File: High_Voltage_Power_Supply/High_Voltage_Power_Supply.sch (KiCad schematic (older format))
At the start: 108 parts, among them J1 Conn_01x02_Female, J2 Conn_01x02_Female, J3 Conn_01x02_Female, J4 Conn_01x12_Female, Q1 Q_NMOS_GDS, Q2 Q_NMOS_GDS, Q3 Q_NMOS_GDS, Q4 Q_NIGBT_GCE, U1 LT3751-TSSOP, U10 ADR3412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

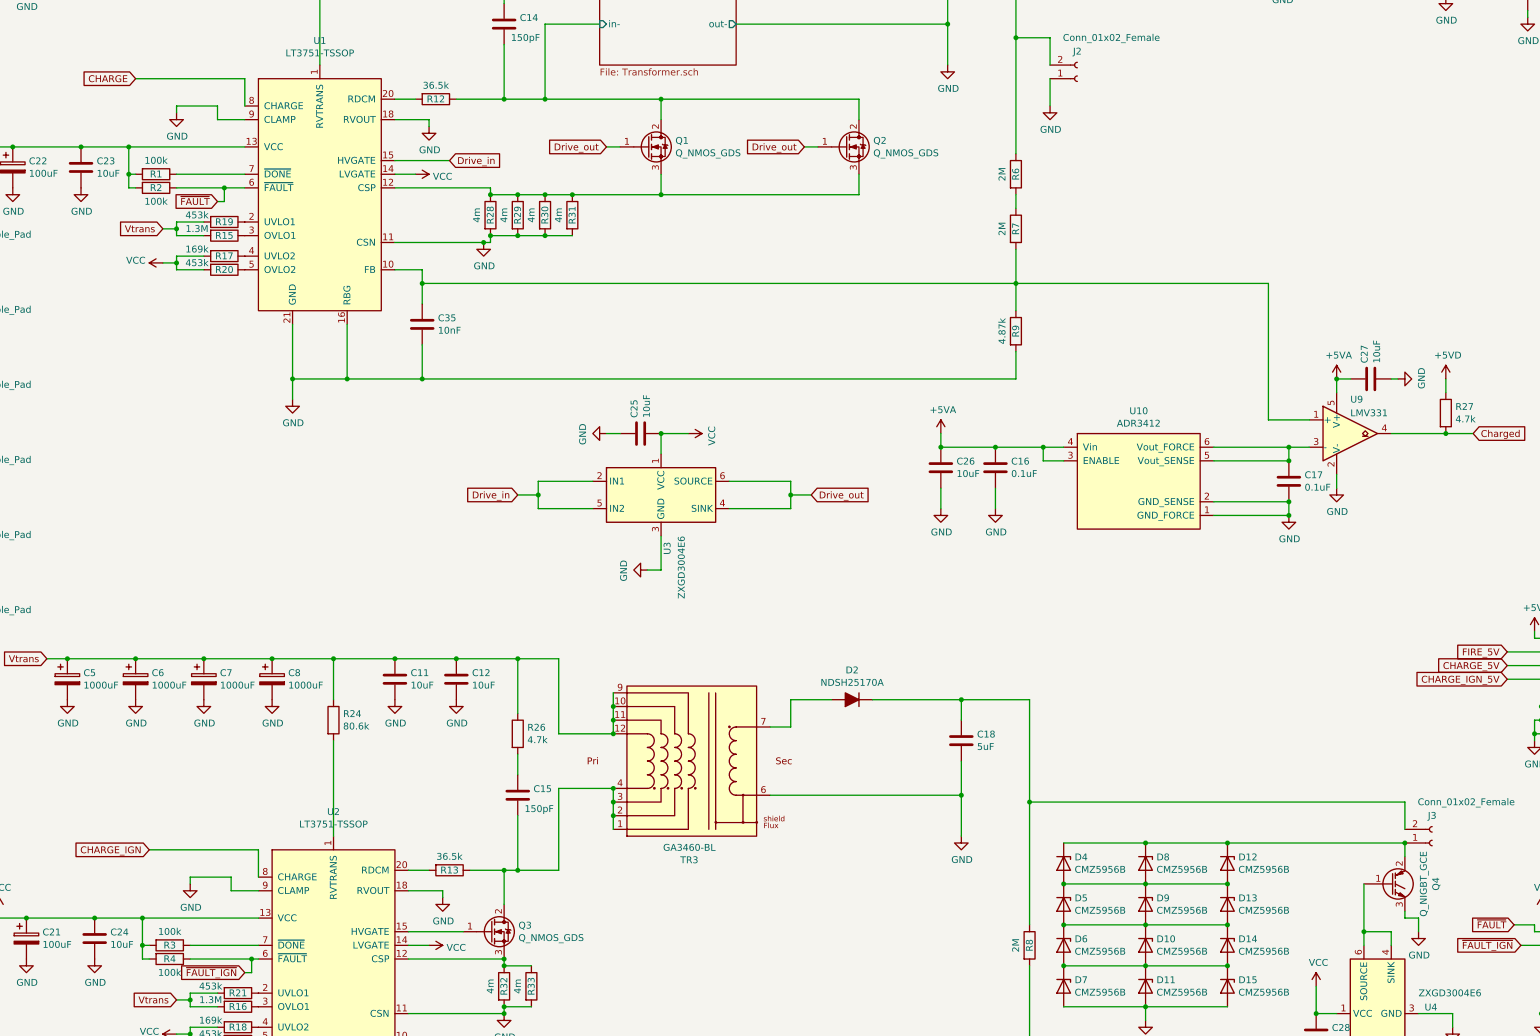
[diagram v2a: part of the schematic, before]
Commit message: Updated component list and schematic for v4
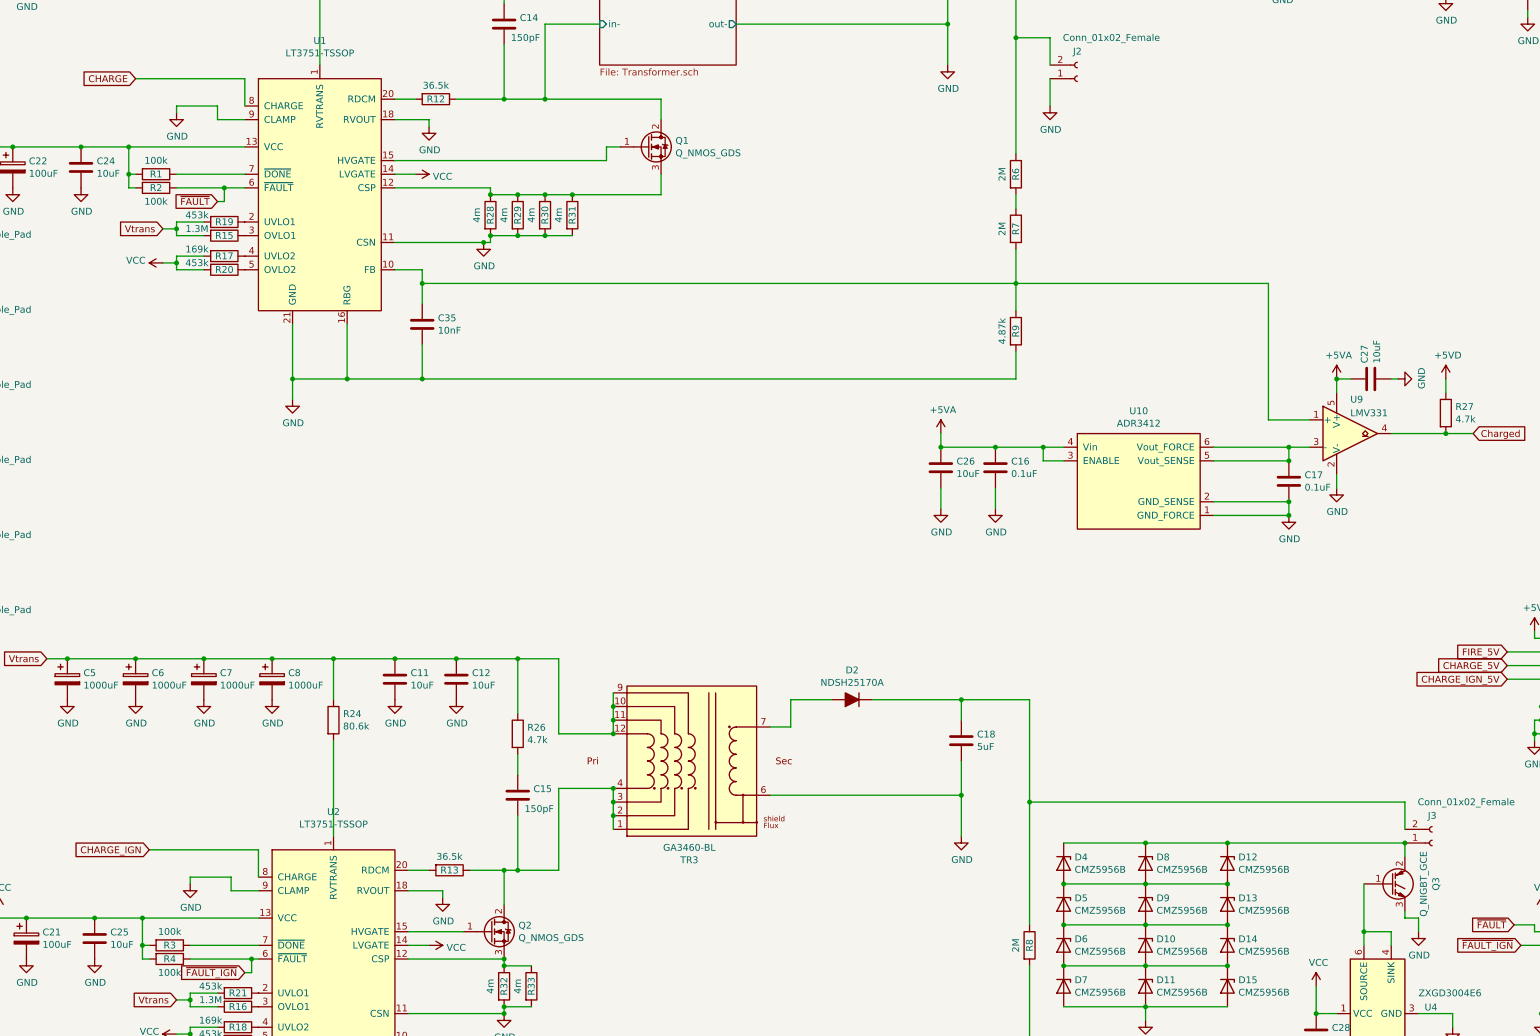
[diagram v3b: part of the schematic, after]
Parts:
- removed C25: 10uF, Capacitor_SMD:C_1206_3216Metric, symbol Device:C
- removed Q2: Q_NMOS_GDS, Package_TO_SOT_THT:TO-264-3_Vertical, symbol Device:Q_NMOS_GDS
- removed U3: ZXGD3004E6, Package_TO_SOT_SMD:SOT-23-6, symbol Driver_FET:ZXGD3004E6
- Q3: renamed from Q4; Link https://www.digikey.com/en/products/detail/ixys/IXYX140N90C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 -> https://www.digikey.com/en/products/detail/ixys/IXYH50N120C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
- renumbered C23 to C24, C24 to C25, Q3 to Q2
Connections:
- net Drive_out is gone; now on an unnamed net: Q1.1 (G)
- net Drive_in: no longer names the net of U1.15 (HVGATE)
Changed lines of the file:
@@
 	4200 2400 4350 2400
 $Comp
-L Device:C C23
+L Device:C C24
 U 1 1 5B8A9F27
 P 1900 2900
-F 0 "C23" H 2015 2946 50  0000 L CNN
+F 0 "C24" H 2015 2946 50  0000 L CNN
 F 1 "10uF" H 2015 2855 50  0000 L CNN
 F 2 "Capacitor_SMD:C_1206_3216Metric" H 1938 2750 50  0001 C CNN
@@
 Wire Wire Line
 	2250 2950 2250 2750
-Wire Wire Line
-	4200 2850 4600 2850
 $Comp
 L power:VCC #PWR0108
@@
 	4300 8050 4450 8050
 $Comp
-L Device:C C24
+L Device:C C25
 U 1 1 5F8F500E
 P 2000 8550
-F 0 "C24" H 2115 8596 50  0000 L CNN
+F 0 "C25" H 2115 8596 50  0000 L CNN
 F 1 "10uF" H 2115 8505 50  0000 L CNN
 F 2 "Capacitor_SMD:C_1206_3216Metric" H 2038 8400 50  0001 C CNN
@@
 $EndComp
 $Comp
-L Device:Q_NMOS_GDS Q3
+L Device:Q_NMOS_GDS Q2
 U 1 1 5F8F5081
 P 4900 8500
-F 0 "Q3" H 5105 8546 50  0000 L CNN
+F 0 "Q2" H 5105 8546 50  0000 L CNN
 F 1 "Q_NMOS_GDS" H 5105 8455 50  0000 L CNN
 F 2 "Package_TO_SOT_THT:TO-264-3_Vertical" H 5100 8600 50  0001 C CNN
@@
 	10950 9100 11100 9100
 $Comp
-L Device:Q_NIGBT_GCE Q4
+L Device:Q_NIGBT_GCE Q3
 U 1 1 5F9A2B3D
 P 11500 8150
-F 0 "Q4" V 11828 8150 50  0000 C CNN
+F 0 "Q3" V 11828 8150 50  0000 C CNN
 F 1 "Q_NIGBT_GCE" V 11737 8150 50  0000 C CNN
 F 2 "Package_TO_SOT_THT:TO-247-3_Vertical" H 11700 8250 50  0001 C CNN
-F 3 "https://www.littelfuse.com/~/media/electronics/datasheets/discrete_igbts/littelfuse_discrete_igbts_xpt_ixy_140n90c3_datasheet.pdf.pdf" H 11500 8150 50  0001 C CNN
-F 4 "https://www.digikey.com/en/products/detail/ixys/IXYX140N90C3/4321711" V 11500 8150 50  0001 C CNN "Link"
+F 3 "https://www.littelfuse.com/~/media/electronics/datasheets/discrete_igbts/littelfuse_discrete_igbts_xpt_ixyh50n120c3d1_datasheet.pdf.pdf" H 11500 8150 50  0001 C CNN
+F 4 "https://www.digikey.com/en/products/detail/ixys/IXYH50N120C3D1/3586445" V 11500 8150 50  0001 C CNN "Link"
 F 5 ">600V" V 11500 8150 50  0001 C CNN "Voltage "
 	1    11500 8150
@@
 	5300 2400 6150 2400
 Connection ~ 5300 2400
-$Comp
-L Driver_FET:ZXGD3004E6 U3
-U 1 1 60A07AB2
-P 6150 5300
-F 0 "U3" V 6196 4956 50  0000 R CNN
-F 1 "ZXGD3004E6" V 6300 5000 50  0000 R CNN
-F 2 "Package_TO_SOT_SMD:SOT-23-6" H 6150 4800 50  0001 C CNN
-F 3 "http://www.diodes.com/_files/datasheets/ZXGD3004E6.pdf" H 5800 5550 50  0001 C CNN
-F 4 "https://www.digikey.com/en/products/detail/diodes-incorporated/ZXGD3004E6TA/1827737?s=N4IgTCBcDaIFoA0DiARAzABgwFgKIDYQBdAXyA" V 6150 5300 50  0001 C CNN "Link"
-	1    6150 5300
-	1    0    0    -1
-$EndComp
-Wire Wire Line
-	5650 5200 5250 5200
-Wire Wire Line
-	5650 5400 5250 5400
-$Comp
-L power:GND #PWR0150
-U 1 1 60A07ABF
-P 6050 5850
-F 0 "#PWR0150" H 6050 5600 50  0001 C CNN
-F 1 "GND" H 6055 5677 50  0000 C CNN
-F 2 "" H 6050 5850 50  0001 C CNN
-F 3 "" H 6050 5850 50  0001 C CNN
-	1    6050 5850
-	0    1    1    0
-$EndComp
-Wire Wire Line
-	6150 5600 6150 5850
-Wire Wire Line
-	6150 5850 6050 5850
-$Comp
-L power:VCC #PWR0151
-U 1 1 60A07AC7
-P 6350 4850
-F 0 "#PWR0151" H 6350 4700 50  0001 C CNN
-F 1 "VCC" H 6367 5023 50  0000 C CNN
-F 2 "" H 6350 4850 50  0001 C CNN
-F 3 "" H 6350 4850 50  0001 C CNN
-	1    6350 4850
-	0    1    1    0
-$EndComp
-Wire Wire Line
-	6350 4850 6150 4850
-Wire Wire Line
-	6150 4850 6150 5000
-Text GLabel 4600 2850 2    50   Input ~ 0
-Drive_in
-Text GLabel 5100 5300 0    50   Input ~ 0
-Drive_in
-Wire Wire Line
-	5250 5200 5250 5300
-Wire Wire Line
-	5100 5300 5250 5300
-Connection ~ 5250 5300
-Wire Wire Line
-	5250 5300 5250 5400
-Wire Wire Line
-	6650 5200 7100 5200
-Wire Wire Line
-	7100 5200 7100 5300
-Wire Wire Line
-	7100 5400 6650 5400
-Text GLabel 7250 5300 2    50   Input ~ 0
-Drive_out
-Wire Wire Line
-	7250 5300 7100 5300
-Connection ~ 7100 5300
-Wire Wire Line
-	7100 5300 7100 5400
-Text GLabel 5750 2750 0    50   Input ~ 0
-Drive_out
 Wire Wire Line
 	5750 2750 5850 2750
-$Comp
-L Device:Q_NMOS_GDS Q2
-U 1 1 60AF002A
-P 7500 2750
-F 0 "Q2" H 7705 2796 50  0000 L CNN
-F 1 "Q_NMOS_GDS" H 7705 2705 50  0000 L CNN
-F 2 "Package_TO_SOT_THT:TO-264-3_Vertical" H 7700 2850 50  0001 C CNN
-F 3 "http://ixapps.ixys.com/DataSheet/DS100129A(IXFK-FX180N25T).pdf" H 7500 2750 50  0001 C CNN
-F 4 "200V" H 7500 2750 50  0001 C CNN "Voltage"
-F 5 "https://www.digikey.com/product-detail/en/ixys/IXFK180N25T/IXFK180N25T-ND/2126319" H 7500 2750 50  0001 C CNN "Link"
-	1    7500 2750
-	1    0    0    -1
-$EndComp
-Text GLabel 7200 2750 0    50   Input ~ 0
-Drive_out
-Wire Wire Line
-	7200 2750 7300 2750
 Wire Wire Line
 	6150 2550 6150 2400
-Connection ~ 6150 2400
 Wire Wire Line
 	6150 2950 6150 3100
-Connection ~ 6150 3100
-Wire Wire Line
-	7600 2550 7600 2400
-Wire Wire Line
-	6150 2400 7600 2400
-Wire Wire Line
-	7600 2950 7600 3100
-Wire Wire Line
-	6150 3100 7600 3100
 Connection ~ 4850 3450
 Wire Wire Line
@@
 	1    0    0    -1
 $EndComp
-$Comp
-L Device:C C25
-U 1 1 612505E4
-P 6000 4850
-F 0 "C25" H 6115 4896 50  0000 L CNN
-F 1 "10uF" H 6115 4805 50  0000 L CNN
-F 2 "Capacitor_SMD:C_1206_3216Metric" H 6038 4700 50  0001 C CNN
-F 3 "https://search.murata.co.jp/Ceramy/image/img/A01X/G101/ENG/GRT31CR61H106KE01-01.pdf" H 6000 4850 50  0001 C CNN
-F 4 "https://www.digikey.com/en/products/detail/murata-electronics/GRT31CR61H106KE01L/5416878" H 6000 4850 50  0001 C CNN "Link"
-F 5 ">50V" H 6000 4850 50  0001 C CNN "Voltage"
-	1    6000 4850
-	0    -1   -1   0
-$EndComp
-Connection ~ 6150 4850
-$Comp
-L power:GND #PWR0164
-U 1 1 612619A2
-P 5750 4850
-F 0 "#PWR0164" H 5750 4600 50  0001 C CNN
-F 1 "GND" H 5755 4677 50  0000 C CNN
-F 2 "" H 5750 4850 50  0001 C CNN
-F 3 "" H 5750 4850 50  0001 C CNN
-	1    5750 4850
-	0    1    1    0
-$EndComp
-Wire Wire Line
-	5850 4850 5750 4850
 $Comp
 L Device:C C14
@@
 	1    0    0    -1
 $EndComp
+Wire Wire Line
+	5750 2850 5750 2750
+Wire Wire Line
+	4200 2850 5750 2850
 $EndSCHEMATC

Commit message: Component updates for new version
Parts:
- removed C16, C17: 0.1uF, Capacitor_SMD:C_1206_3216Metric, symbol Device:C
- removed C26, C27, C32, C33: 10uF, Capacitor_SMD:C_1206_3216Metric, symbol Device:C
- removed C6, C7, C8: 1000uF, Capacitor_THT:CP_Radial_D18.0mm_P7.50mm, symbol Device:CP
- removed D10, D11, D12, D13, D14, D15, D4, D5, D6, D7, D8, D9: CMZ5956B, Diode_SMD:D_SMA, symbol Device:D_Zener
- removed H3, H4: MountingHole_Pad, MountingHole:MountingHole_3.2mm_M3_Pad_Via, symbol Mechanical:MountingHole_Pad
- removed R27: 4.7k, Resistor_SMD:R_1206_3216Metric, symbol Device:R
- removed U10: ADR3412, Package_TO_SOT_SMD:SOT-23-6, symbol High_Voltage_Power_Supply:ADR3412
- removed U8: LM7805, Package_TO_SOT_SMD:SOT-223-3_TabPin2, symbol Regulator_Linear:LM7805_TO220
- removed U9: LMV331, Package_TO_SOT_SMD:SOT-353_SC-70-5, symbol Comparator:LMV331
- renumbered C24 to C26, C25 to C27, H5 to H3, H6 to H4
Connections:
- net Charged is gone; now on net +5VD: J4.7 (Pin_7)
- net +5VD: no longer J4.5 (Pin_5)
- net VCC: now also J4.5 (Pin_5)
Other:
- moved on the sheet: C4, C5, H3, H4

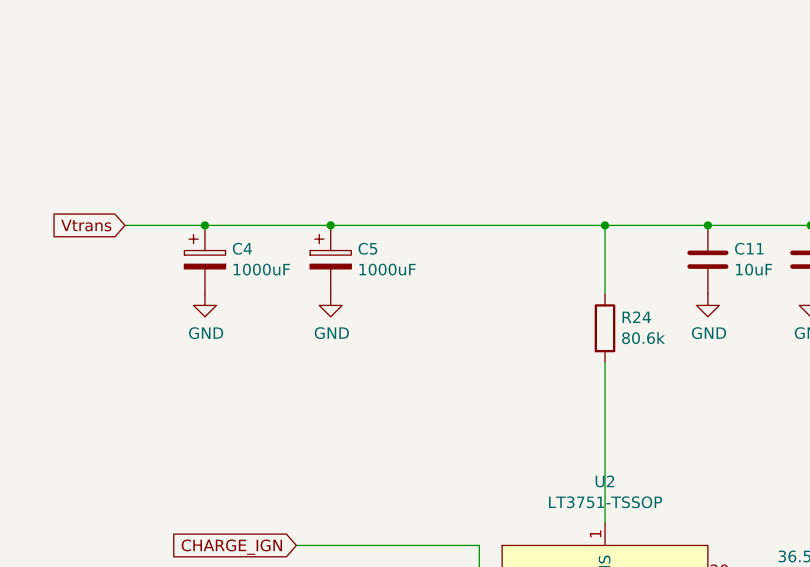
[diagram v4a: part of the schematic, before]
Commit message: updated components to match new requirements from experiments
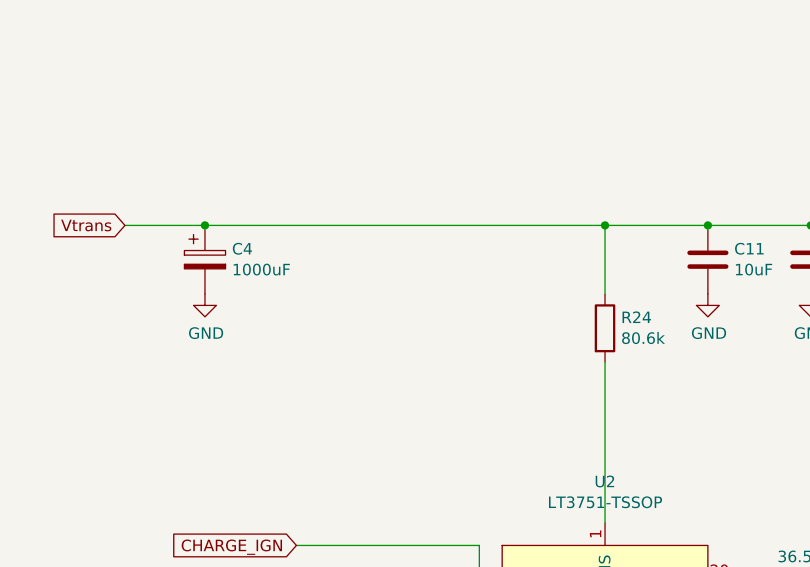
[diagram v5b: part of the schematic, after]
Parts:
- removed C5: 1000uF, Capacitor_THT:CP_Radial_D18.0mm_P7.50mm, symbol Device:CP
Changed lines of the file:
@@
 	1    0    0    -1
 $EndComp
-$Comp
-L power:GND #PWR0146
-U 1 1 60771EEA
-P 2550 6800
-F 0 "#PWR0146" H 2550 6550 50  0001 C CNN
-F 1 "GND" H 2555 6627 50  0000 C CNN
-F 2 "" H 2550 6800 50  0001 C CNN
-F 3 "" H 2550 6800 50  0001 C CNN
-	1    2550 6800
-	1    0    0    -1
-$EndComp
-$Comp
-L Device:CP C5
-U 1 1 6076EBA7
-P 2550 6650
-F 0 "C5" H 2668 6696 50  0000 L CNN
-F 1 "1000uF" H 2668 6605 50  0000 L CNN
-F 2 "Capacitor_THT:CP_Radial_D18.0mm_P7.50mm" H 2588 6500 50  0001 C CNN
-F 3 "http://nichicon-us.com/english/products/pdfs/e-upw.pdf" H 2550 6650 50  0001 C CNN
-F 4 "https://www.digikey.com/product-detail/en/nichicon/UPW2A102MHD/493-1988-ND/589729" H 2550 6650 50  0001 C CNN "Link"
-	1    2550 6650
-	1    0    0    -1
-$EndComp
-Connection ~ 2550 6500
-Wire Wire Line
-	2550 6500 3750 6500
 Wire Wire Line
 	1650 6500 2000 6500
 Connection ~ 2000 6500
 Wire Wire Line
-	2000 6500 2550 6500
+	2700 850  3650 850
 Wire Wire Line
-	2700 850  3650 850
+	2000 6500 3750 6500
 $EndSCHEMATC
